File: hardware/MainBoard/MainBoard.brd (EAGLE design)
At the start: 90 x 56 mm, 265 parts, among them J1 CON-71741-2184-BOT, J2 CON-71741-2184-TOP, J3 CON-FTSH-105-01-L-DV-K, J4 CON-ZX62R-B-5P, J7 CON-RJ45-J0G-0007NL, J8 SWITCH-CJS-1200-1200, M1 MOUNT-HOLE3.3, M2 MOUNT-HOLE3.3, M3 MOUNT-HOLE3.3, M4 MOUNT-HOLE3.3, M5 FIDUCIAL1X2, M6 FIDUCIAL1X2, M7 FIDUCIAL1X2, M8 FIDUCIAL1X2, Q1 MMBT3904, SW1 SWITCH-ESWITCH-TL3340G, SW2 SWITCH-ESWITCH-TL3340G, U1 A2F500M3G-1FGG256, U2 MAX19706-T4877-4, U3 MAX19706-T4877-4, U4 USBLC6-2SC6, U5 FT232HL, U6 DP83848C-VBH48A, U7 93LC56BT-OT, U8 DS1818-10-SOT-23, X1 ECX-2236-200, X2 ECX-31B, X3 ASEM1-C, X5 ECX-42-120

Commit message: Cleaned up schematic after the review.
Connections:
- net AGND: now also J1.35, J1.36, J1.41, J1.42, J1.47, J1.48, J1.53, J1.54, J1.59, J1.60, J1.65, J1.66, J1.71, J1.72
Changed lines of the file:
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@@
 <wire x1="56.75" y1="39.5" x2="56.75" y2="34.5" width="0.3048" layer="2"/>
 <wire x1="50.5" y1="39.5" x2="56.75" y2="39.5" width="0.3048" layer="2"/>
+<contactref element="J1" pad="36"/>
+<contactref element="J1" pad="35"/>
+<contactref element="J1" pad="47"/>
+<contactref element="J1" pad="48"/>
+<contactref element="J1" pad="54"/>
+<contactref element="J1" pad="53"/>
+<contactref element="J1" pad="59"/>
+<contactref element="J1" pad="60"/>
+<contactref element="J1" pad="65"/>
+<contactref element="J1" pad="66"/>
+<contactref element="J1" pad="71"/>
+<contactref element="J1" pad="72"/>
+<contactref element="J1" pad="41"/>
+<contactref element="J1" pad="42"/>
+<wire x1="50.5" y1="48.9" x2="51.5" y2="48.9" width="0" layer="19" extent="16-16"/>
+<wire x1="49.5" y1="48.9" x2="50.5" y2="48.9" width="0" layer="19" extent="16-16"/>
+<wire x1="48.5" y1="48.9" x2="49.5" y2="48.9" width="0" layer="19" extent="16-16"/>
+<wire x1="47.5" y1="48.9" x2="48.5" y2="48.9" width="0" layer="19" extent="16-16"/>
+<wire x1="45.5" y1="48.9" x2="46.5" y2="48.9" width="0" layer="19" extent="16-16"/>
+<wire x1="44.5" y1="48.9" x2="45.5" y2="48.9" width="0" layer="19" extent="16-16"/>
+<wire x1="43.5" y1="48.9" x2="44.5" y2="48.9" width="0" layer="19" extent="16-16"/>
+<wire x1="47.45" y1="50.35" x2="47.5" y2="48.9" width="0" layer="19" extent="1-16"/>
+<wire x1="42.15" y1="49.7" x2="43.5" y2="48.9" width="0" layer="19" extent="1-16"/>
+<wire x1="43" y1="52.65" x2="42" y2="52.75" width="0" layer="19" extent="1-1"/>
+<wire x1="41" y1="52.65" x2="42" y2="52.75" width="0" layer="19" extent="1-1"/>
+<wire x1="41" y1="48.9" x2="42" y2="49.75" width="0" layer="19" extent="1-16"/>
+<wire x1="40.85" y1="48" x2="41" y2="48.9" width="0" layer="19" extent="1-16"/>
+<wire x1="41" y1="45.4" x2="40.5" y2="45.5" width="0" layer="19" extent="1-16"/>
+<wire x1="42" y1="45.4" x2="41" y2="45.4" width="0" layer="19" extent="16-16"/>
+<wire x1="39.5" y1="46.5" x2="40.5" y2="46.5" width="0" layer="19" extent="1-1"/>
+<wire x1="39" y1="45.4" x2="39.5" y2="45.5" width="0" layer="19" extent="1-16"/>
+<wire x1="38" y1="45.4" x2="39" y2="45.4" width="0" layer="19" extent="16-16"/>
+<wire x1="42.5" y1="43.5" x2="42" y2="45.4" width="0" layer="19" extent="1-16"/>
+<wire x1="44" y1="42.15" x2="43" y2="43" width="0" layer="19" extent="1-16"/>
+<wire x1="46" y1="42" x2="44.85" y2="43" width="0" layer="19" extent="16-16"/>
+<wire x1="46.5" y1="41.5" x2="46" y2="42" width="0" layer="19" extent="1-1"/>
+<wire x1="40.5" y1="43.5" x2="41" y2="45.4" width="0" layer="19" extent="1-16"/>
+<wire x1="39" y1="52.65" x2="41" y2="52.65" width="0" layer="19" extent="1-1"/>
+<wire x1="37.75" y1="52.75" x2="39" y2="52.65" width="0" layer="19" extent="1-1"/>
+<wire x1="36.5" y1="52.65" x2="37.75" y2="52.75" width="0" layer="19" extent="1-1"/>
+<wire x1="48.5" y1="43.5" x2="47" y2="42" width="0" layer="19" extent="1-1"/>
+<wire x1="49.5" y1="45.5" x2="49" y2="44" width="0" layer="19" extent="1-1"/>
+<wire x1="45.85" y1="45" x2="44.85" y2="43" width="0" layer="19" extent="16-16"/>
+<wire x1="45.5" y1="45.5" x2="45.85" y2="45" width="0" layer="19" extent="1-16"/>
+<wire x1="38.5" y1="48.9" x2="40.5" y2="47.55" width="0" layer="19" extent="1-16"/>
+<wire x1="52.5" y1="43.5" x2="49.5" y2="43.5" width="0" layer="19" extent="1-1"/>
+<wire x1="59.5" y1="8.85" x2="59.5" y2="8.85" width="0" layer="19" extent="1-16"/>
+<wire x1="56.5" y1="8.85" x2="56.5" y2="8.85" width="0" layer="19" extent="1-16"/>
+<wire x1="59.5" y1="5.15" x2="59.5" y2="5.15" width="0" layer="19" extent="1-16"/>
+<wire x1="53.5" y1="8.85" x2="53.5" y2="8.85" width="0" layer="19" extent="1-16"/>
+<wire x1="56.5" y1="5.15" x2="56.5" y2="5.15" width="0" layer="19" extent="1-16"/>
+<wire x1="53.5" y1="5.15" x2="53.5" y2="5.15" width="0" layer="19" extent="1-16"/>
+<wire x1="50.5" y1="8.85" x2="50.5" y2="8.85" width="0" layer="19" extent="1-16"/>
+<wire x1="47.5" y1="8.85" x2="47.5" y2="8.85" width="0" layer="19" extent="1-16"/>
+<wire x1="50.5" y1="5.15" x2="50.5" y2="5.15" width="0" layer="19" extent="1-16"/>
+<wire x1="47.5" y1="5.15" x2="47.5" y2="5.15" width="0" layer="19" extent="1-16"/>
+<wire x1="44.5" y1="8.85" x2="44.5" y2="8.85" width="0" layer="19" extent="1-16"/>
+<wire x1="41.5" y1="8.85" x2="41.5" y2="8.85" width="0" layer="19" extent="1-16"/>
+<wire x1="44.5" y1="5.15" x2="44.5" y2="5.15" width="0" layer="19" extent="1-16"/>
+<wire x1="41.5" y1="5.15" x2="41.5" y2="5.15" width="0" layer="19" extent="1-16"/>
+<wire x1="54.4" y1="44.5" x2="53.25" y2="43.5" width="0" layer="19" extent="1-16"/>
+<wire x1="54.15" y1="12.25" x2="53.5" y2="10.5" width="0" layer="19" extent="1-1"/>
+<wire x1="54.25" y1="13.1" x2="54.15" y2="12.25" width="0" layer="19" extent="1-16"/>
+<wire x1="55.25" y1="13.1" x2="54.25" y2="13.1" width="0" layer="19" extent="16-16"/>
+<wire x1="55.5" y1="13.65" x2="55.25" y2="13.1" width="0" layer="19" extent="1-16"/>
+<wire x1="53.25" y1="13.1" x2="54.25" y2="13.1" width="0" layer="19" extent="16-16"/>
+<wire x1="52.25" y1="13.1" x2="53.25" y2="13.1" width="0" layer="19" extent="16-16"/>
+<wire x1="51.5" y1="13.65" x2="52.25" y2="13.1" width="0" layer="19" extent="1-16"/>
+<wire x1="56.5" y1="13.1" x2="55.5" y2="13.65" width="0" layer="19" extent="1-16"/>
+<wire x1="57.5" y1="13.1" x2="56.5" y2="13.1" width="0" layer="19" extent="16-16"/>
+<wire x1="58.15" y1="12.25" x2="57.5" y2="13.1" width="0" layer="19" extent="1-16"/>
+<wire x1="59.5" y1="13.25" x2="58.15" y2="12.25" width="0" layer="19" extent="1-1"/>
+<wire x1="60.4" y1="15.25" x2="59.5" y2="14.35" width="0" layer="19" extent="1-16"/>
+<wire x1="40.85" y1="12.25" x2="41.5" y2="10.5" width="0" layer="19" extent="1-1"/>
+<wire x1="40.5" y1="13.1" x2="40.85" y2="12.25" width="0" layer="19" extent="1-16"/>
+<wire x1="41.5" y1="13.1" x2="40.5" y2="13.1" width="0" layer="19" extent="16-16"/>
+<wire x1="42.5" y1="13.1" x2="41.5" y2="13.1" width="0" layer="19" extent="16-16"/>
+<wire x1="43.5" y1="13.65" x2="42.5" y2="13.1" width="0" layer="19" extent="1-16"/>
+<wire x1="44.5" y1="13.6" x2="43.5" y2="13.65" width="0" layer="19" extent="1-1"/>
+<wire x1="43.5" y1="14.75" x2="43.5" y2="13.65" width="0" layer="19" extent="1-1"/>
+<wire x1="39.5" y1="13.65" x2="40.5" y2="13.1" width="0" layer="19" extent="1-16"/>
+<wire x1="39.25" y1="13.1" x2="39.5" y2="13.65" width="0" layer="19" extent="1-16"/>
+<wire x1="38.25" y1="13.1" x2="39.25" y2="13.1" width="0" layer="19" extent="16-16"/>
+<wire x1="37.25" y1="12.1" x2="38.25" y2="13.1" width="0" layer="19" extent="16-16"/>
+<wire x1="36.85" y1="12.25" x2="37.25" y2="12.1" width="0" layer="19" extent="1-16"/>
+<wire x1="36.25" y1="12.1" x2="36.85" y2="12.25" width="0" layer="19" extent="1-16"/>
+<wire x1="44.9" y1="16.25" x2="43.5" y2="14.75" width="0" layer="19" extent="16-16"/>
+<wire x1="54.75" y1="15.75" x2="55.5" y2="13.65" width="0" layer="19" extent="1-1"/>
+<wire x1="53.4" y1="19.75" x2="54.25" y2="19.25" width="0" layer="19" extent="1-16"/>
+<wire x1="56.85" y1="18.75" x2="55.75" y2="19.25" width="0" layer="19" extent="1-16"/>
+<wire x1="56.85" y1="20.75" x2="55.25" y2="20.25" width="0" layer="19" extent="1-16"/>
+<wire x1="58.5" y1="22.75" x2="56.85" y2="21.75" width="0" layer="19" extent="1-16"/>
+<wire x1="38.75" y1="15.75" x2="39.5" y2="13.65" width="0" layer="19" extent="1-1"/>
+<wire x1="37.4" y1="19.5" x2="38.25" y2="19.25" width="0" layer="19" extent="1-16"/>
+<wire x1="37.4" y1="20.5" x2="37.4" y2="19.5" width="0" layer="19" extent="16-16"/>
+<wire x1="40.85" y1="18.75" x2="39.75" y2="19.25" width="0" layer="19" extent="1-16"/>
+<wire x1="40.85" y1="17.75" x2="40.85" y2="18.75" width="0" layer="19" extent="16-16"/>
+<wire x1="40.85" y1="20.75" x2="39.25" y2="20.25" width="0" layer="19" extent="1-16"/>
+<wire x1="40.85" y1="21.75" x2="40.85" y2="20.75" width="0" layer="19" extent="16-16"/>
+<wire x1="42.5" y1="22.75" x2="40.85" y2="21.75" width="0" layer="19" extent="1-16"/>
+<wire x1="62.5" y1="14.35" x2="60.4" y2="15.25" width="0" layer="19" extent="1-16"/>
+<wire x1="62.15" y1="20" x2="59.75" y2="20.25" width="0" layer="19" extent="1-1"/>
+<wire x1="62.15" y1="22.25" x2="62.15" y2="20" width="0" layer="19" extent="1-16"/>
+<wire x1="62.15" y1="23" x2="62.15" y2="22.25" width="0" layer="19" extent="1-16"/>
+<wire x1="62.15" y1="23.25" x2="62.15" y2="23" width="0" layer="19" extent="1-16"/>
+<wire x1="46.15" y1="20" x2="43.75" y2="20.25" width="0" layer="19" extent="1-1"/>
+<wire x1="48.35" y1="19.75" x2="46.15" y2="20" width="0" layer="19" extent="1-16"/>
+<wire x1="48.35" y1="18.75" x2="48.35" y2="19.75" width="0" layer="19" extent="16-16"/>
+<wire x1="46.15" y1="22.25" x2="46.15" y2="20" width="0" layer="19" extent="1-16"/>
+<wire x1="46.15" y1="23" x2="46.15" y2="22.25" width="0" layer="19" extent="1-16"/>
+<wire x1="46.15" y1="23.25" x2="46.15" y2="23" width="0" layer="19" extent="1-16"/>
+<wire x1="34.6" y1="14" x2="36.25" y2="12.1" width="0" layer="19" extent="16-16"/>
+<wire x1="34.25" y1="16.35" x2="34.6" y2="14" width="0" layer="19" extent="16-16"/>
+<wire x1="47.5" y1="14.35" x2="44.5" y2="13.6" width="0" layer="19" extent="1-1"/>
 </signal>
 <signal name="VBUS">

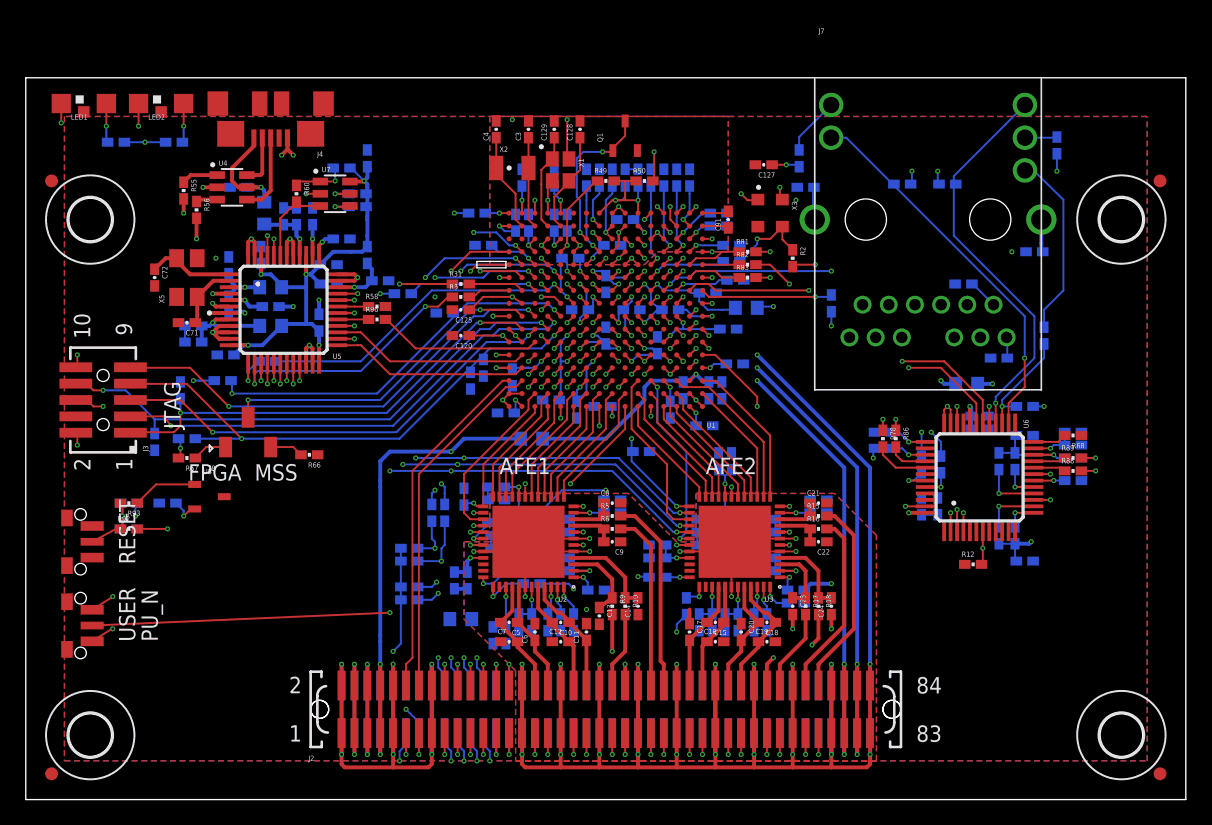
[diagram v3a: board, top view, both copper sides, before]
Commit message: Modified push-button area.
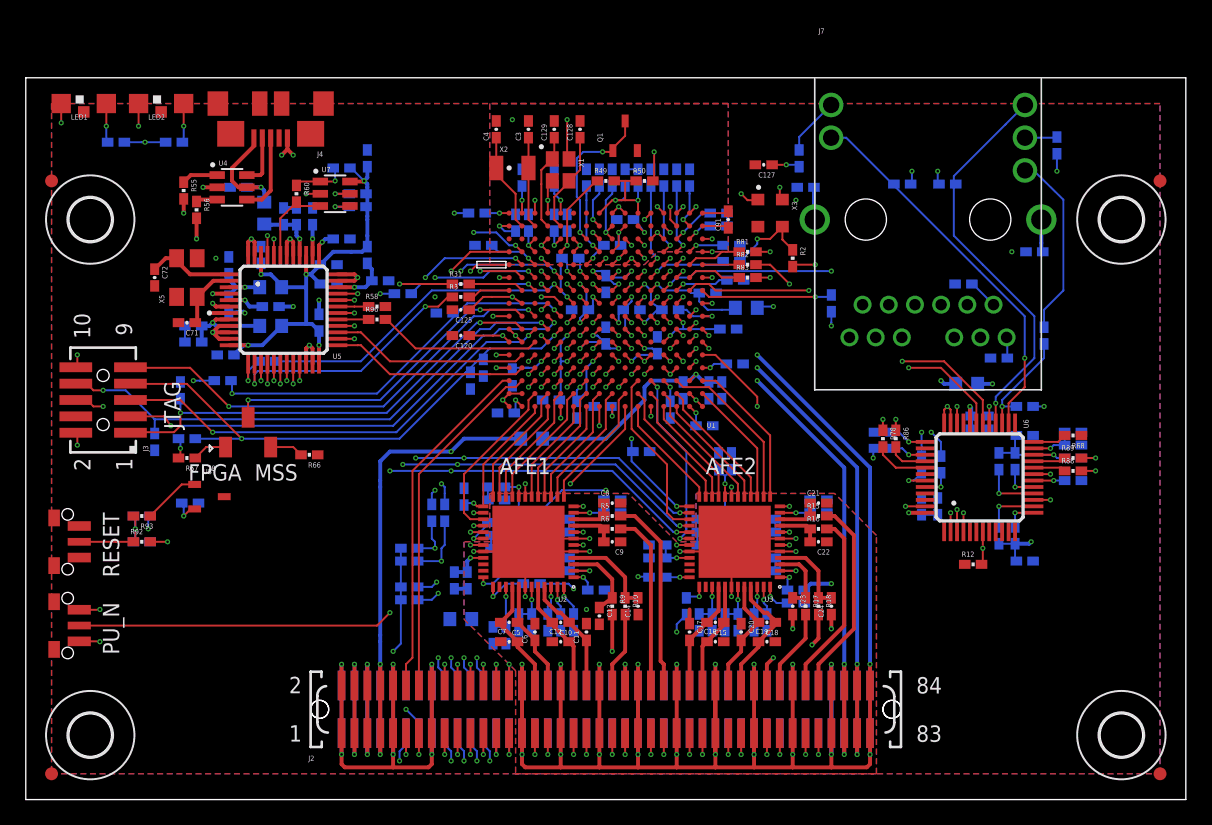
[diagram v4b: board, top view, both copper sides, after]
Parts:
- moved C130 1.75 mm to (12.8, 23.0), turned to 180 degrees
- moved C90 1.41 mm to (9.00, 20.0)
- moved R91 1.41 mm to (9.00, 22.0)
- moved R92 1.41 mm to (9.00, 20.0)
- moved R93 1.41 mm to (9.00, 22.0)
- moved SW1 1.00 mm to (1.75, 20.0)
- moved SW2 1.00 mm to (1.75, 13.5)
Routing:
- net !MSS_RESET_PB: track 6.70 -> 8.45 mm
- net !WAKEUP: track 79.3 -> 80.7 mm
- net DGND: track 144.3 -> 143.6 mm
- net !MSS_RESET: track 110.4 -> 111.0 mm
- net EXTIC-RST: track 5.05 -> 4.46 mm
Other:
- board text removed: "1mm closer to board edge?"
- board text removed: "USER"

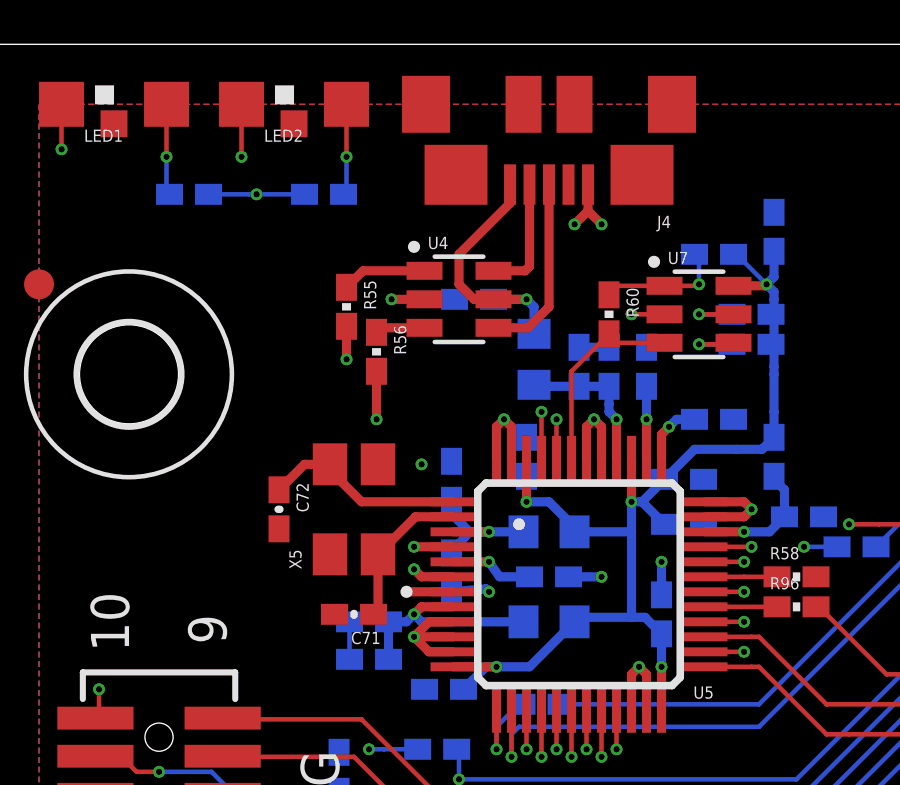
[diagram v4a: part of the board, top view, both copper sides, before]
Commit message: 
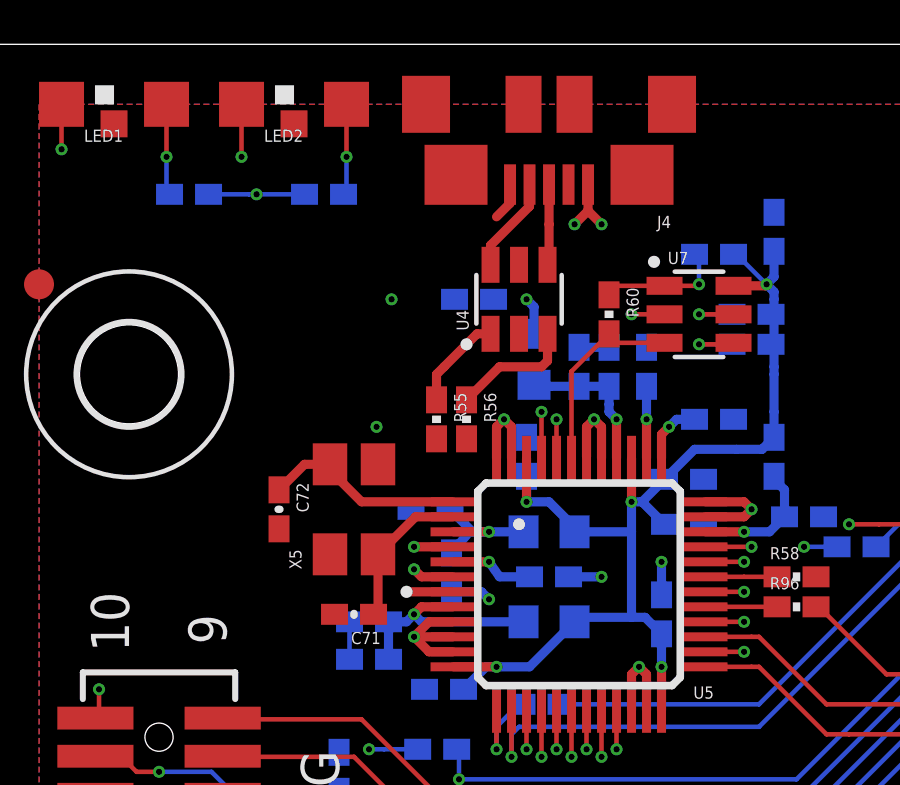
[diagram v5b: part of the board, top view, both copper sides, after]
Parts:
- moved R55 4.80 mm to (15.2, 43.5)
- moved R56 3.75 mm to (16.2, 43.5)
- moved U4 2.00 mm to (18.0, 47.5), turned to 90 degrees
- moved C97 1.18 mm to (15.1, 40.5), turned to 0 degrees
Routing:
- net USBDM: track 10.4 -> 1.40 mm, vias 2 -> 1
- net USBDP: track 9.31 -> 1.55 mm, vias 2 -> 1
- net VBUS: track 8.84 -> 2.51 mm
- net USBDP-IN: track 6.21 -> 2.70 mm
- net USBDP-OUT: track 1.66 -> 4.14 mm
- net USBDM-IN: track 4.29 -> 3.21 mm
- net DGND: track 143.6 -> 142.6 mm

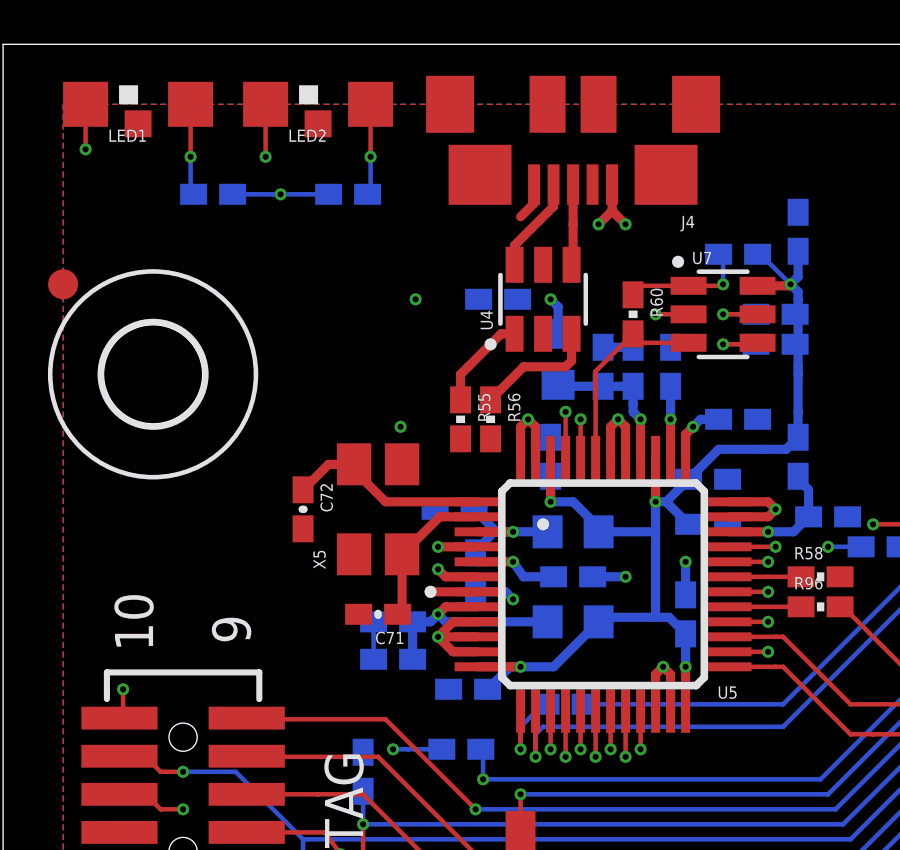
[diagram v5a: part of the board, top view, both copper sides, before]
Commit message: Rerouted the USB data signals.
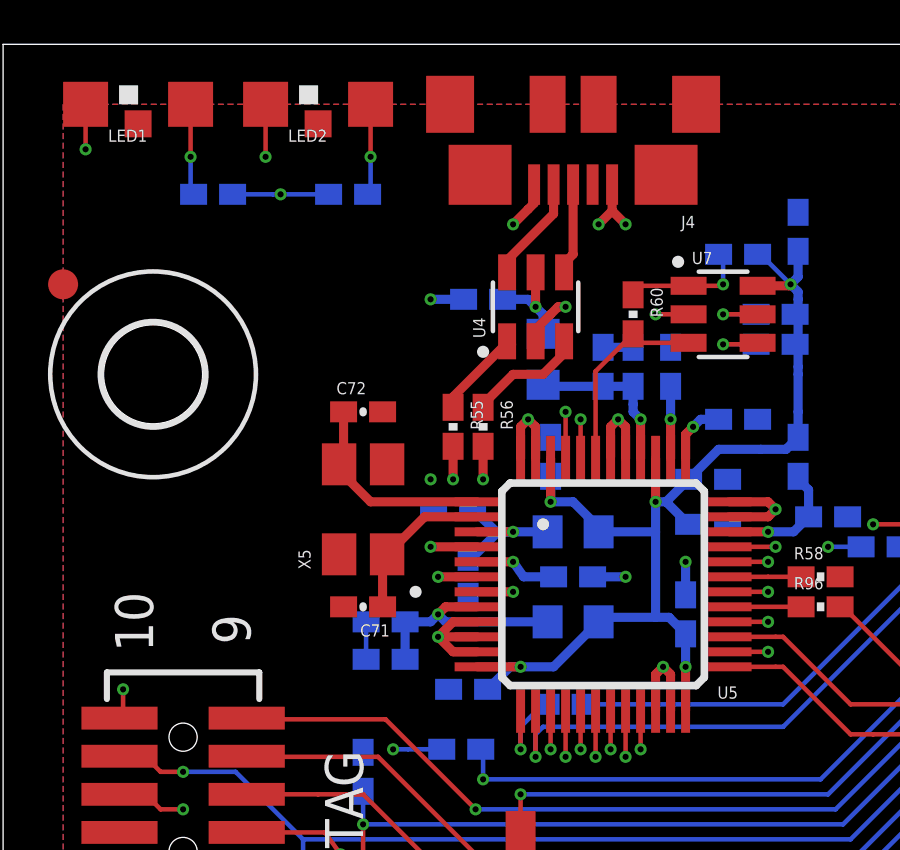
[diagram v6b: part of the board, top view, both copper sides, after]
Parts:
- moved C72 3.82 mm to (12.0, 43.8), turned to 0 degrees
- moved C71 0.56 mm to (12.0, 37.2)
- moved B2 0.50 mm to (18.0, 45.5)
- moved C92 0.50 mm to (16.0, 47.5)
- moved X5 0.50 mm to (12.0, 40.5)
- moved R55 0.35 mm to (15.0, 43.2)
- moved R56 0.35 mm to (16.0, 43.2)
- moved U4 0.35 mm to (17.8, 47.2)
- moved C96 0.29 mm to (15.5, 38.2)
- moved C98 0.25 mm to (12.8, 35.5)
- moved C99 0.25 mm to (12.8, 36.8)
- moved C97 0.05 mm to (15.0, 40.5)
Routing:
- net VBUS: track 2.51 -> 8.15 mm, vias 1 -> 2
- net USBDP: track 1.55 -> 6.46 mm, vias 1 -> 2
- net USBDM: track 1.40 -> 5.86 mm, vias 1 -> 2
- net DGND: track 142.6 -> 145.1 mm
- net UXCSI: track 6.87 -> 7.62 mm
- net VREGIN: track 5.01 -> 5.52 mm
